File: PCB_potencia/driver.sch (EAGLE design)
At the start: 38 parts, among them Q1 IRF530, Q2 IRF530, Q3 IRF530, T1 BC547, T2 BC547, T3 2SC1815, T4 2SC1815, T5 BC547, T6 BC547, T7 BC547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

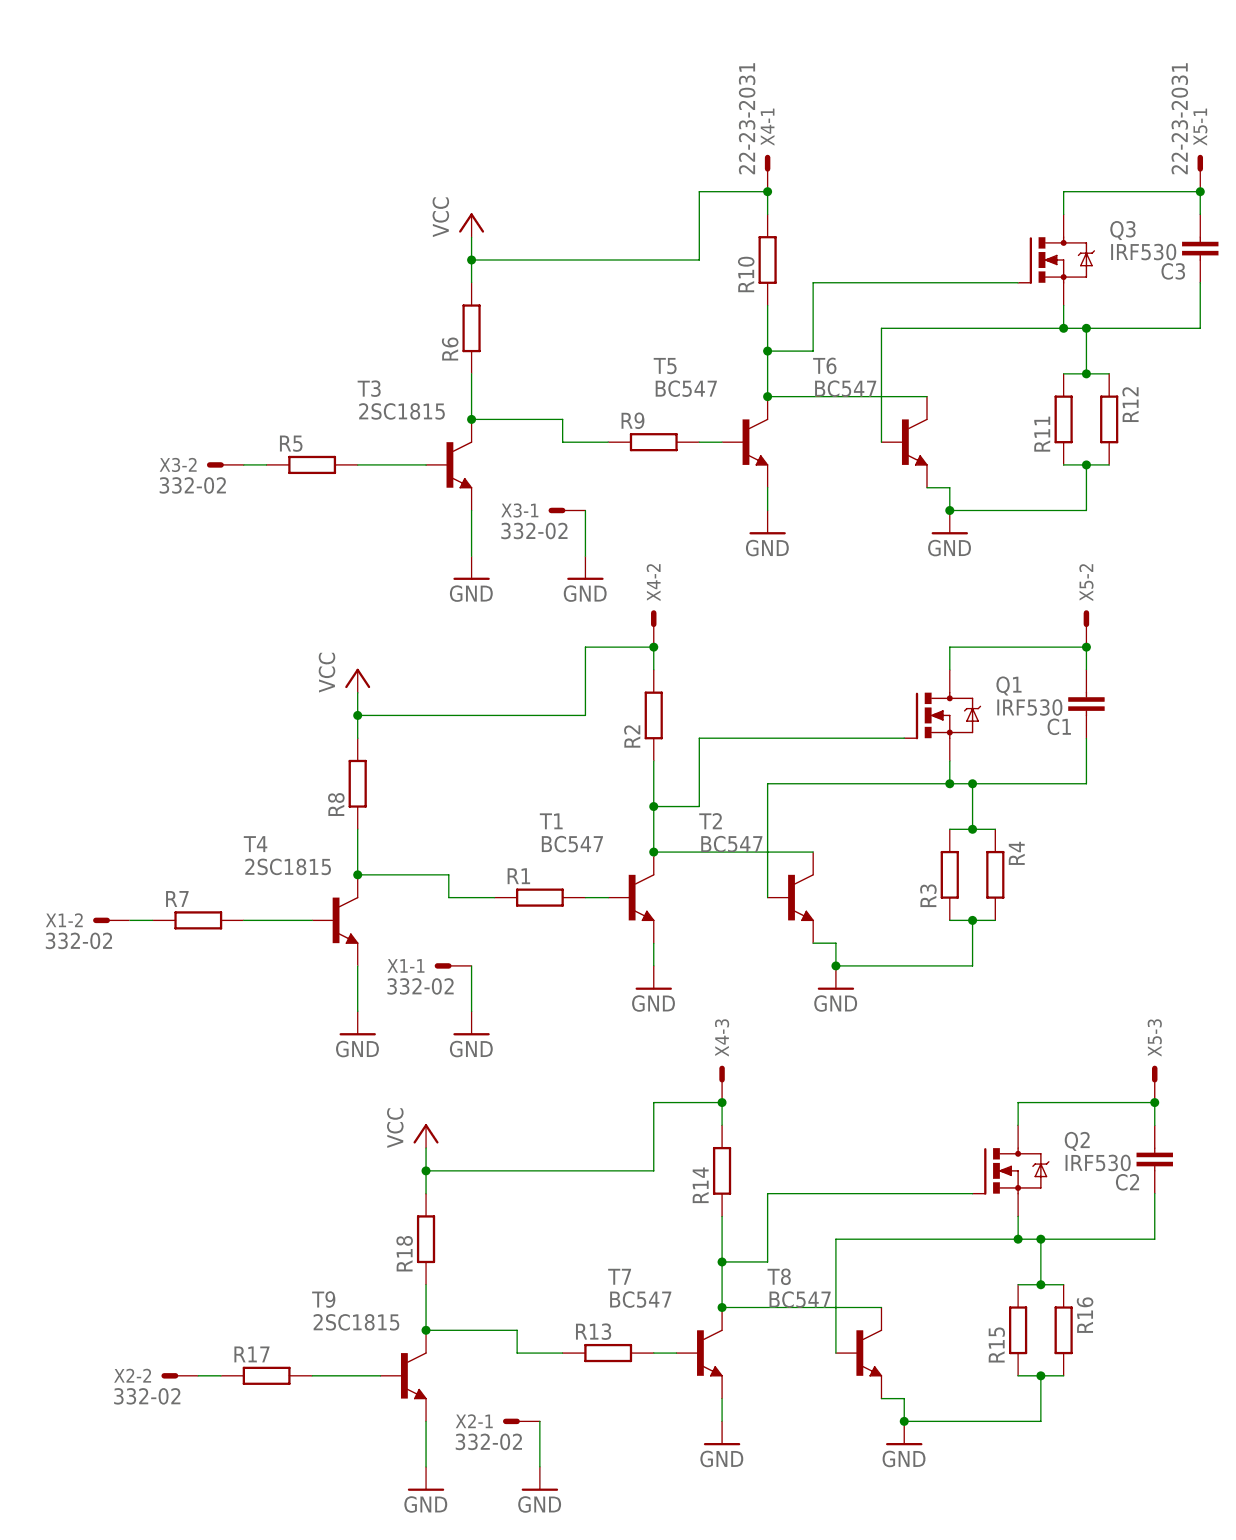
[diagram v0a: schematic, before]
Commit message: Se corrige transistor para invertir la señal de cada PWM y se ajustan resistencias de potencia
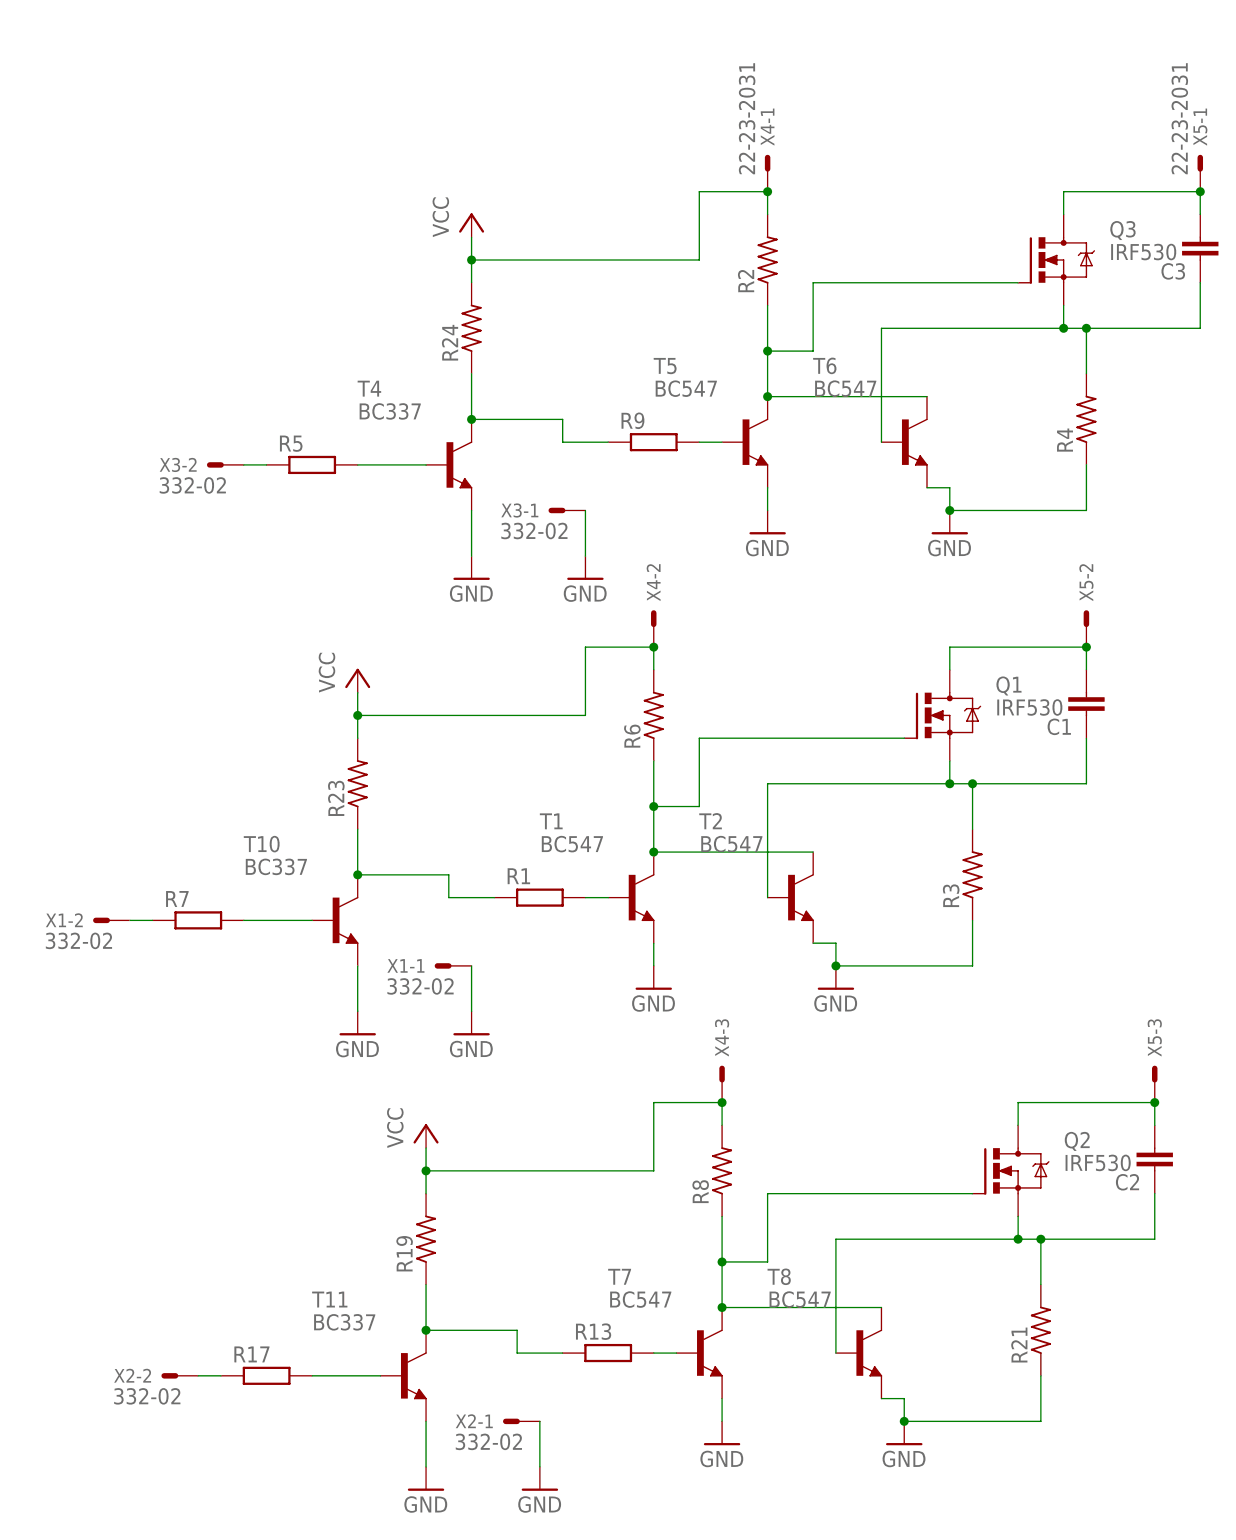
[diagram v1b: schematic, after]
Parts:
- removed R10, R11, R12, R14, R15, R16: (no value), eagle-ltspice:R0204/7
- removed R18: (no value), rcl:R-EU_0204/7
- removed T3, T9: 2SC1815, transistor:2SC1815
- added R19, R23, R24: (no value), resistor:R-US_0309/10
- added R21: (no value), resistor:R-US_0817/22
- added T10, T11: BC337, transistor:BC337
- R2: device eagle-ltspice:R0204/7 -> resistor:R-US_0309/10
- R3, R4: device eagle-ltspice:R0204/7 -> resistor:R-US_0817/22
- R6, R8: device rcl:R-EU_0204/7 -> resistor:R-US_0309/10
- T4: value 2SC1815 -> BC337; device transistor:2SC1815 -> transistor:BC337
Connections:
- net GND: now also R21.1, R4.1, T10.E, T11.E; no longer R11.1, R12.2, R15.1, R16.2, R4.2, T3.E, T9.E
- net N$13: now also R2.1; no longer R10.1
- net N$15: now also R4.2; no longer R11.2, R12.1
- net N$16: now also R8.1; no longer R14.1
- net N$18: now also R21.2; no longer R15.2, R16.1
- net N$19: now also T11.B; no longer T9.B
- net N$2: now also R6.1; no longer R2.1
- net N$20: now also R19.1, T11.C; no longer R18.1, T9.C
- net N$4: now also T4.B; no longer T3.B
- net N$5: no longer R4.1
- net N$6: now also T10.B; no longer T4.B
- net N$7: now also R24.1, T4.C; no longer R6.1, T3.C
- net N$9: now also R23.1, T10.C; no longer R8.1, T4.C
- net VCC: now also R19.2, R23.2, R24.2; no longer R10.2, R14.2, R18.2
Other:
- moved on the sheet: T4
